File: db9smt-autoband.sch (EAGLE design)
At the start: 26 parts, among them CON1 PADONPRINT, CON2 PADONPRINT, CON3 PADONPRINT, CON4 PADONPRINT, CON5 PADONPRINT, CON6 PADONPRINT, CON7 PADONPRINT, CON8 PADONPRINT, CON9 PADONPRINT, IC1 PCA9536

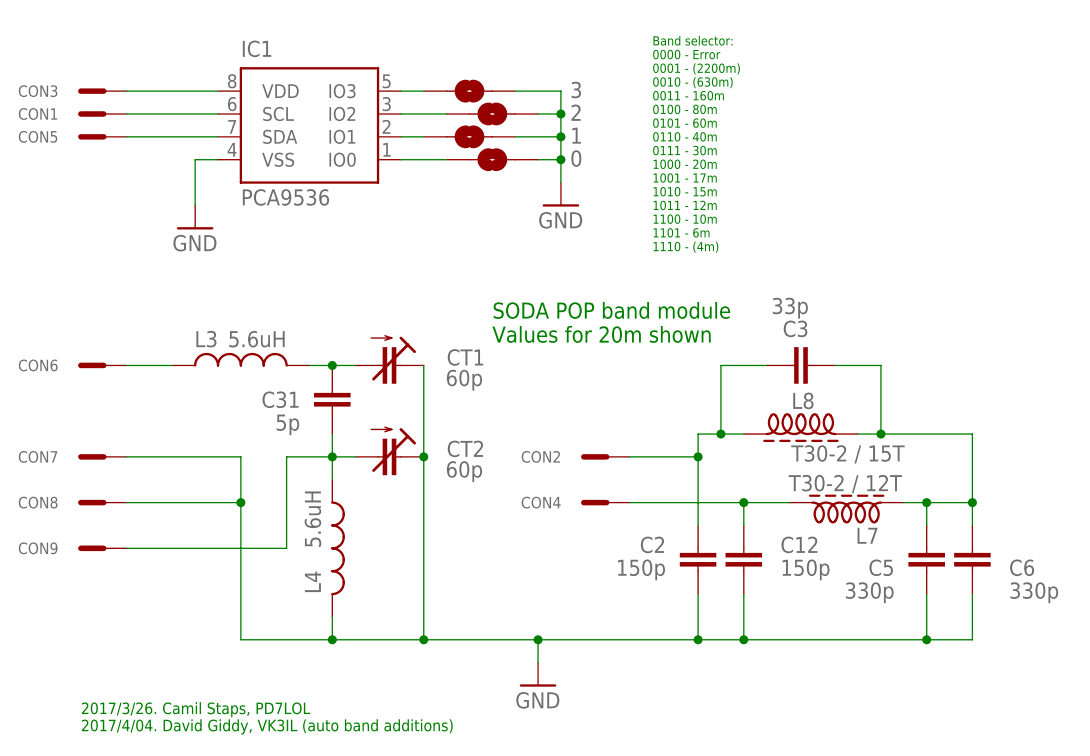
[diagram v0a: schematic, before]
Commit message: Fixed hole size on trimmer cap
Fixed hole size on trimmer cap in library PCA9536.lbr and updated the
two autoband boards to use the corrected package. Package can be
replaced on other boards with the one in this library to fix the
problem. Also moved the text on the horizontal board to the bPlace
layer. Couldn't do this on the smaller board as no where to put it!
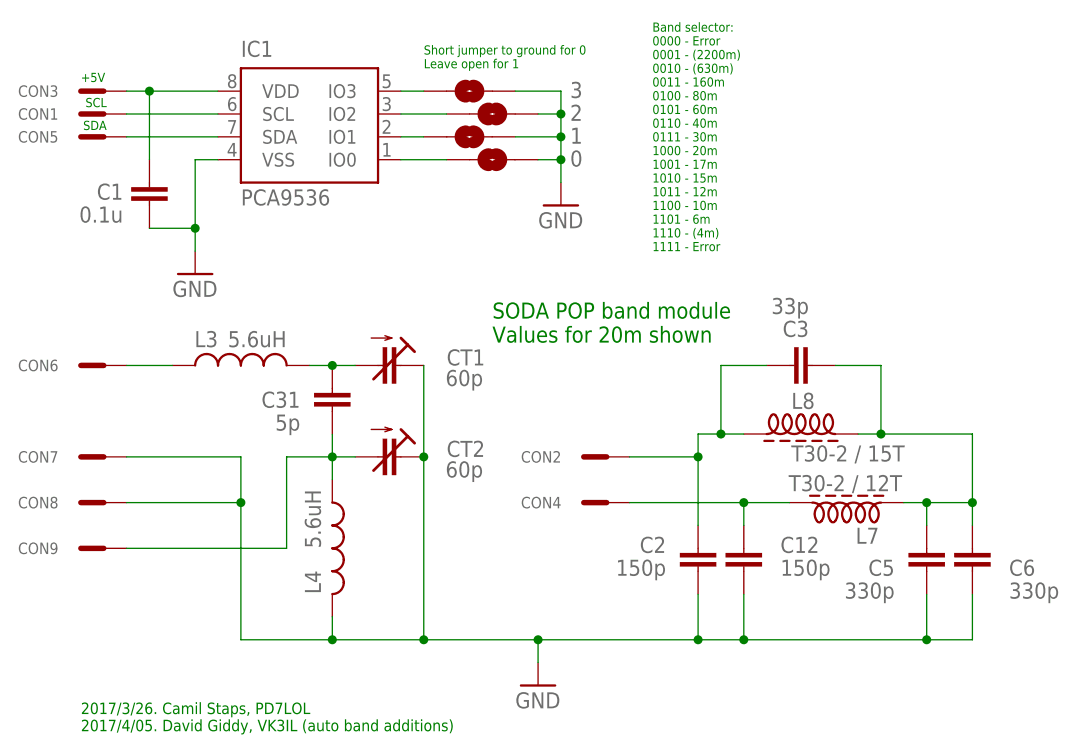
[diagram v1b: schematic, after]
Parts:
- added C1: 0.1u, eagle-ltspice:CC0603
- CT1, CT2: device rcl:C-TRIMMTZ03 -> PCA9536:C-TRIMMTZ03
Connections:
- net GND: now also C1.2
- net N$7: now also C1.1
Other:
- note added: "+5V"
- note added: "2017/3/26. Camil Staps, PD7LOL 2017/4/05. David Giddy, VK3IL (auto band additions)"
- note added: "Band selector: 0000 - Error 0001 - (2200m) 0010 - (630m) 0011 - 160m 0100 - 80m 0101 - 60m 0110 - 40m 0111 - 30m 1000 - 20m 1001 - 17m 1010 - 15m 1011 - 12m 1100 - 10m 1101 - 6m 1110 - (4m) 1111 - Error"
- note added: "SCL"
- note added: "SDA"
- note added: "Short jumper to ground for 0 Leave open for 1"
- note removed: "2017/3/26. Camil Staps, PD7LOL 2017/4/04. David Giddy, VK3IL (auto band additions)"
- note removed: "Band selector: 0000 - Error 0001 - (2200m) 0010 - (630m) 0011 - 160m 0100 - 80m 0101 - 60m 0110 - 40m 0111 - 30m 1000 - 20m 1001 - 17m 1010 - 15m 1011 - 12m 1100 - 10m 1101 - 6m 1110 - (4m)"
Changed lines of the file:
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@@
 </classes>
 <parts>
-<part name="CT1" library="rcl" deviceset="C-TRIMM" device="TZ03" value="60p"/>
-<part name="CT2" library="rcl" deviceset="C-TRIMM" device="TZ03" value="60p"/>
+<part name="CT1" library="PCA9536" deviceset="C-TRIMM" device="TZ03" value="60p"/>
+<part name="CT2" library="PCA9536" deviceset="C-TRIMM" device="TZ03" value="60p"/>
 <part name="L8" library="toroids" deviceset="INDUCTOR" device="T30-2-28AWG-15T" value="T30-2 / 15T"/>
 <part name="L7" library="toroids" deviceset="INDUCTOR" device="T30-2-28AWG-15T" value="T30-2 / 12T"/>
@@
 <part name="0" library="PCA9536" deviceset="SJ" device=""/>
 <part name="GND3" library="supply1" deviceset="GND" device=""/>
+<part name="C1" library="eagle-ltspice" deviceset="C" device="C0603" value="0.1u"/>
 </parts>
 <sheets>
@@
 Values for 20m shown</text>
 <text x="-66.04" y="25.4" size="1.27" layer="91">2017/3/26. Camil Staps, PD7LOL
-2017/4/04. David Giddy, VK3IL (auto band additions)</text>
+2017/4/05. David Giddy, VK3IL (auto band additions)</text>
 <text x="-2.54" y="78.74" size="1.016" layer="91">Band selector:
 0000 - Error
@@
 1100 - 10m
 1101 - 6m
-1110 - (4m)</text>
+1110 - (4m)
+1111 - Error</text>
+<text x="-27.94" y="99.06" size="1.016" layer="91">Short jumper to ground for 0
+Leave open for 1</text>
+<text x="-66.04" y="97.536" size="1.016" layer="91">+5V</text>
+<text x="-65.532" y="94.742" size="1.016" layer="91">SCL</text>
+<text x="-65.786" y="92.202" size="1.016" layer="91">SDA</text>
 </plain>
 <instances>
@@
 </instance>
 <instance part="IC1" gate="P" x="-40.64" y="86.36"/>
-<instance part="GND2" gate="1" x="-53.34" y="81.28"/>
+<instance part="GND2" gate="1" x="-53.34" y="76.2"/>
 <instance part="3" gate="1" x="-22.86" y="96.52" smashed="yes">
 <attribute name="NAME" x="-11.684" y="95.758" size="1.778" layer="95"/>
@@
 </instance>
 <instance part="GND3" gate="1" x="-12.7" y="83.82"/>
+<instance part="C1" gate="G$1" x="-58.42" y="86.36" smashed="yes">
+<attribute name="NAME" x="-61.341" y="85.344" size="1.778" layer="95" rot="R180" align="center-left"/>
+<attribute name="VALUE" x="-61.341" y="82.804" size="1.778" layer="96" rot="R180" align="center-left"/>
+</instance>
 </instances>
 <busses>
@@
 <segment>
 <pinref part="GND2" gate="1" pin="GND"/>
-<wire x1="-53.34" y1="83.82" x2="-53.34" y2="88.9" width="0.1524" layer="91"/>
+<wire x1="-53.34" y1="78.74" x2="-53.34" y2="81.28" width="0.1524" layer="91"/>
 <pinref part="IC1" gate="P" pin="VSS"/>
+<wire x1="-53.34" y1="81.28" x2="-53.34" y2="88.9" width="0.1524" layer="91"/>
 <wire x1="-53.34" y1="88.9" x2="-50.8" y2="88.9" width="0.1524" layer="91"/>
+<pinref part="C1" gate="G$1" pin="2"/>
+<wire x1="-58.42" y1="81.28" x2="-53.34" y2="81.28" width="0.1524" layer="91"/>
+<junction x="-53.34" y="81.28"/>
 </segment>
 <segment>
@@
 <pinref part="CON3" gate="G$1" pin="P$1"/>
 <pinref part="IC1" gate="P" pin="VDD"/>
-<wire x1="-60.96" y1="96.52" x2="-50.8" y2="96.52" width="0.1524" layer="91"/>
-</segment>
-</net>
+<wire x1="-60.96" y1="96.52" x2="-58.42" y2="96.52" width="0.1524" layer="91"/>
+<pinref part="C1" gate="G$1" pin="1"/>
+<wire x1="-58.42" y1="96.52" x2="-50.8" y2="96.52" width="0.1524" layer="91"/>
+<wire x1="-58.42" y1="88.9" x2="-58.42" y2="96.52" width="0.1524" layer="91"/>
+<junction x="-58.42" y="96.52"/>
+</segment>
+</net>
